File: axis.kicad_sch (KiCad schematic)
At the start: 48 parts, among them J101 CORTEX-DEBUG, J102 JAE_DX07S016JA1R1500, SW101 SW_Push, SW102 SW_Push, U101 BHI160, U102 ATSAMD51G, U103 BMM150, U104 AP2112K-3.3, Y101 32.768kHz

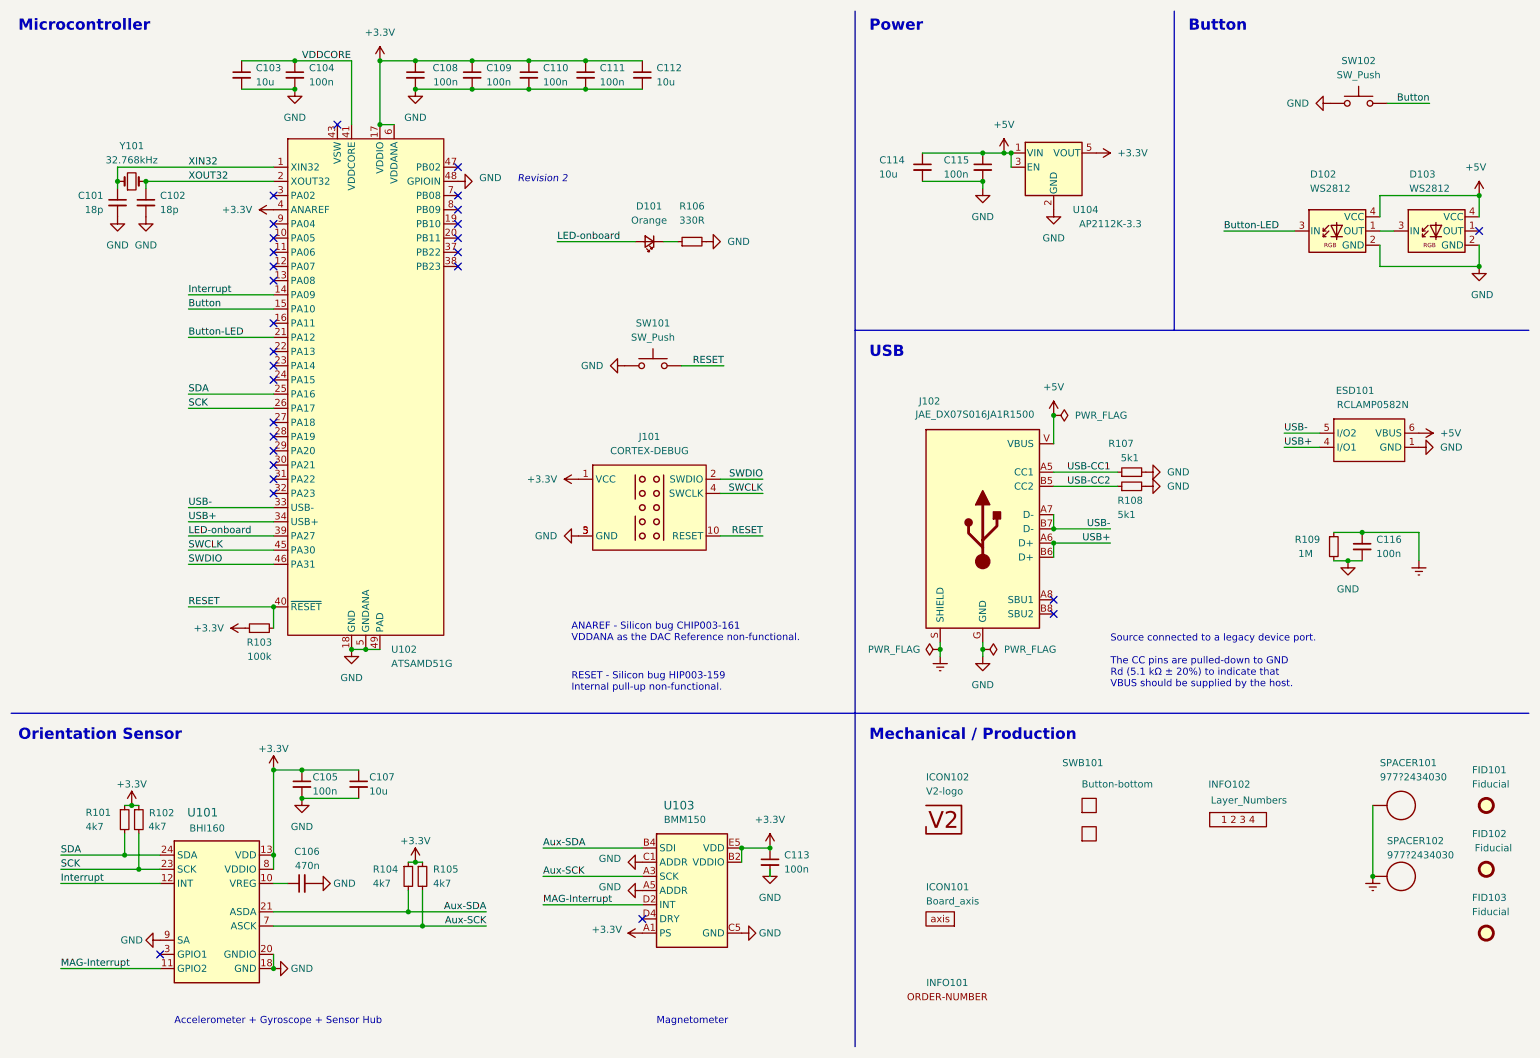
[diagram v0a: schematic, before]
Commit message: Update to KiCat 7.0
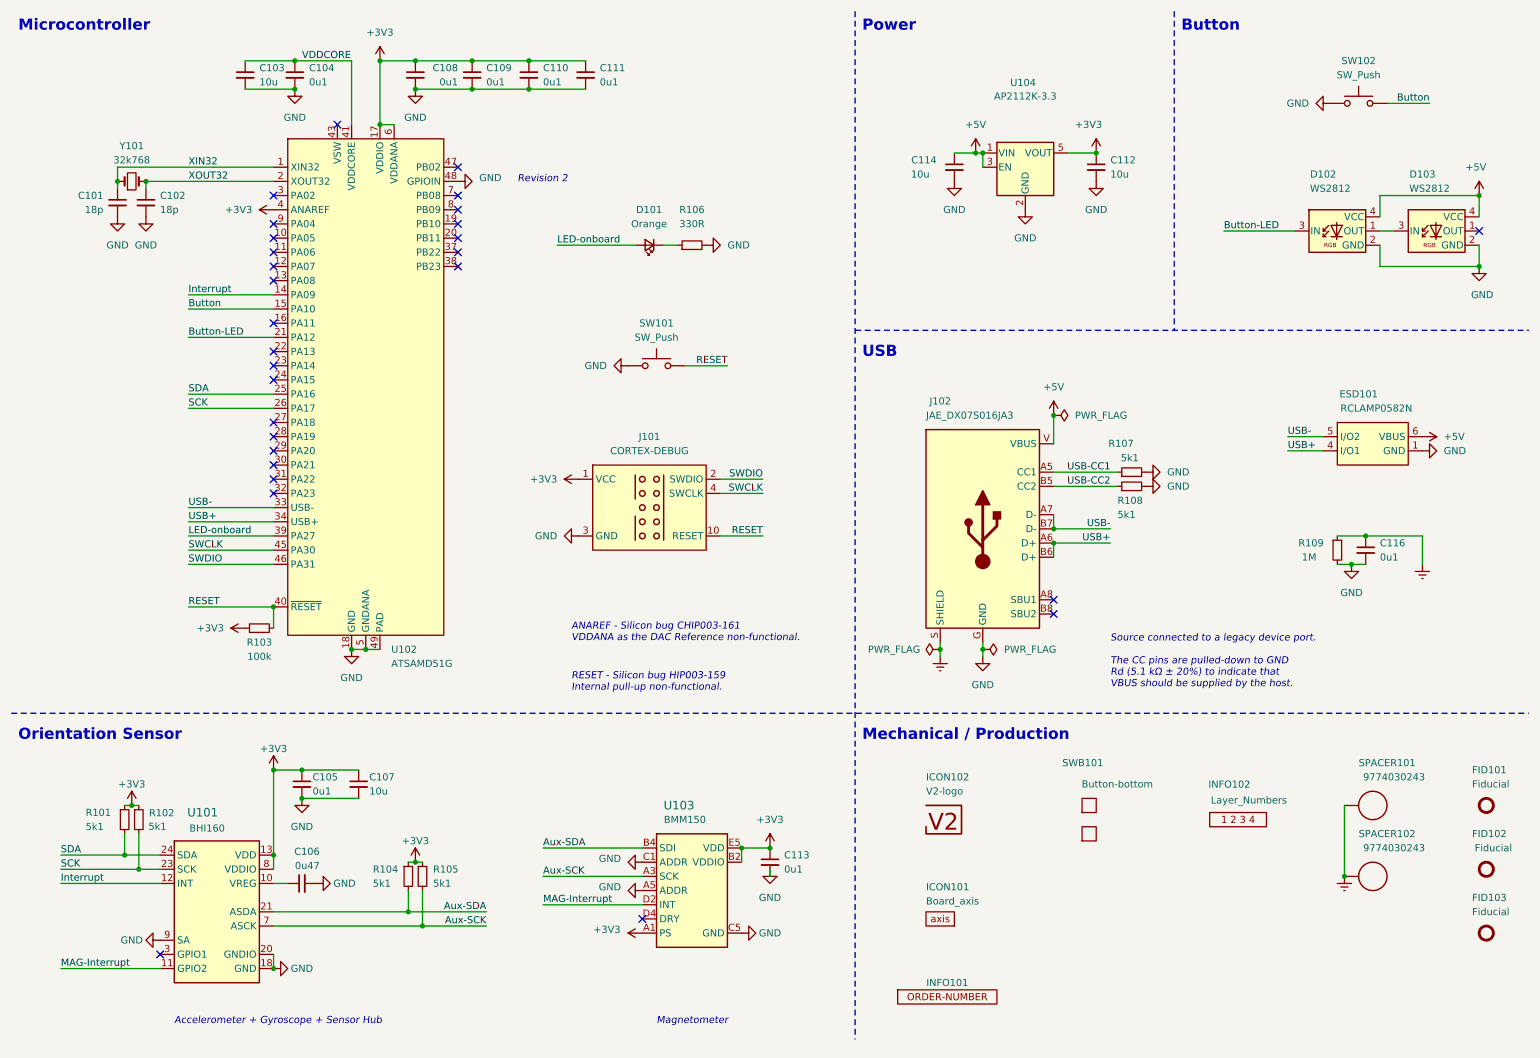
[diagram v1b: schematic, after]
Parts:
- removed C115: 100n, Capacitor_SMD:C_0603_1608Metric, symbol Device:C_Small
- C104, C105, C108, C109, C110, C111, C113, C116: value 100n -> 0u1
- C106: value 470n -> 0u47
- FID101, FID102, FID103: now left out of the parts list
- J102: value JAE_DX07S016JA1R1500 -> JAE_DX07S016JA3; footprint V2_Connector_USB:JAE_DX07S016JA1R1500 -> V2_Connector_USB:JAE_DX07S016JA3; symbol V2_Connector_USB:JAE_DX07S016JA1R1500 -> V2_Connector_USB:JAE_DX07S016JA3
- R101, R102, R104, R105: value 4k7 -> 5k1
- SPACER101, SPACER102: value 977?2434030 -> 9774030243; symbol V2_Spacer_Wurth:977?2434030 -> V2_Spacer_Wurth:9774030243
- Y101: value 32.768kHz -> 32k768
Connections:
- net +3.3V renamed +3V3
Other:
- moved on the sheet: C103, C112, C114, C116, D101, ESD101, R106, R109, SPACER101, SPACER102, SW101, U104

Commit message: Refresh
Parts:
- R101, R102, R104, R105: value 5k1 -> 2k7
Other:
- moved on the sheet: ICON102
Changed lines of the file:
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@@
       (effects (font (size 1.27 1.27)) (justify left))
     )
-    (property "Value" "5k1" (at 37.2867 158.7105 0)
+    (property "Value" "2k7" (at 37.2867 158.7105 0)
       (effects (font (size 1.27 1.27)) (justify left))
     )
@@
       (effects (font (size 1.27 1.27)) (justify left))
     )
-    (property "Value" "5k1" (at 77.47 168.91 0)
+    (property "Value" "2k7" (at 77.47 168.91 0)
       (effects (font (size 1.27 1.27)) (justify left))
     )
@@
       (effects (font (size 1.27 1.27)) (justify left))
     )
-    (property "Value" "5k1" (at 26.035 158.75 0)
+    (property "Value" "2k7" (at 26.035 158.75 0)
       (effects (font (size 1.27 1.27)) (justify left))
     )
@@
       (effects (font (size 1.27 1.27)) (justify left))
     )
-    (property "Value" "5k1" (at 88.265 168.91 0)
-      (effects (font (size 1.27 1.27)) (justify left))
-    )
+    (property "Value" "2k7" (at 88.265 168.91 0)
+      (effects (font (size 1.27 1.27)) (justify left))
+    )
